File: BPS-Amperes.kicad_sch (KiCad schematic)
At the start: 36 parts, among them J1 Conn_02x10_Odd_Even, J2 ShuntConn, U1 INA186A3IDDFT, U2 OPA2196, U3 LTC2315, U4 REF1930AIDDCT

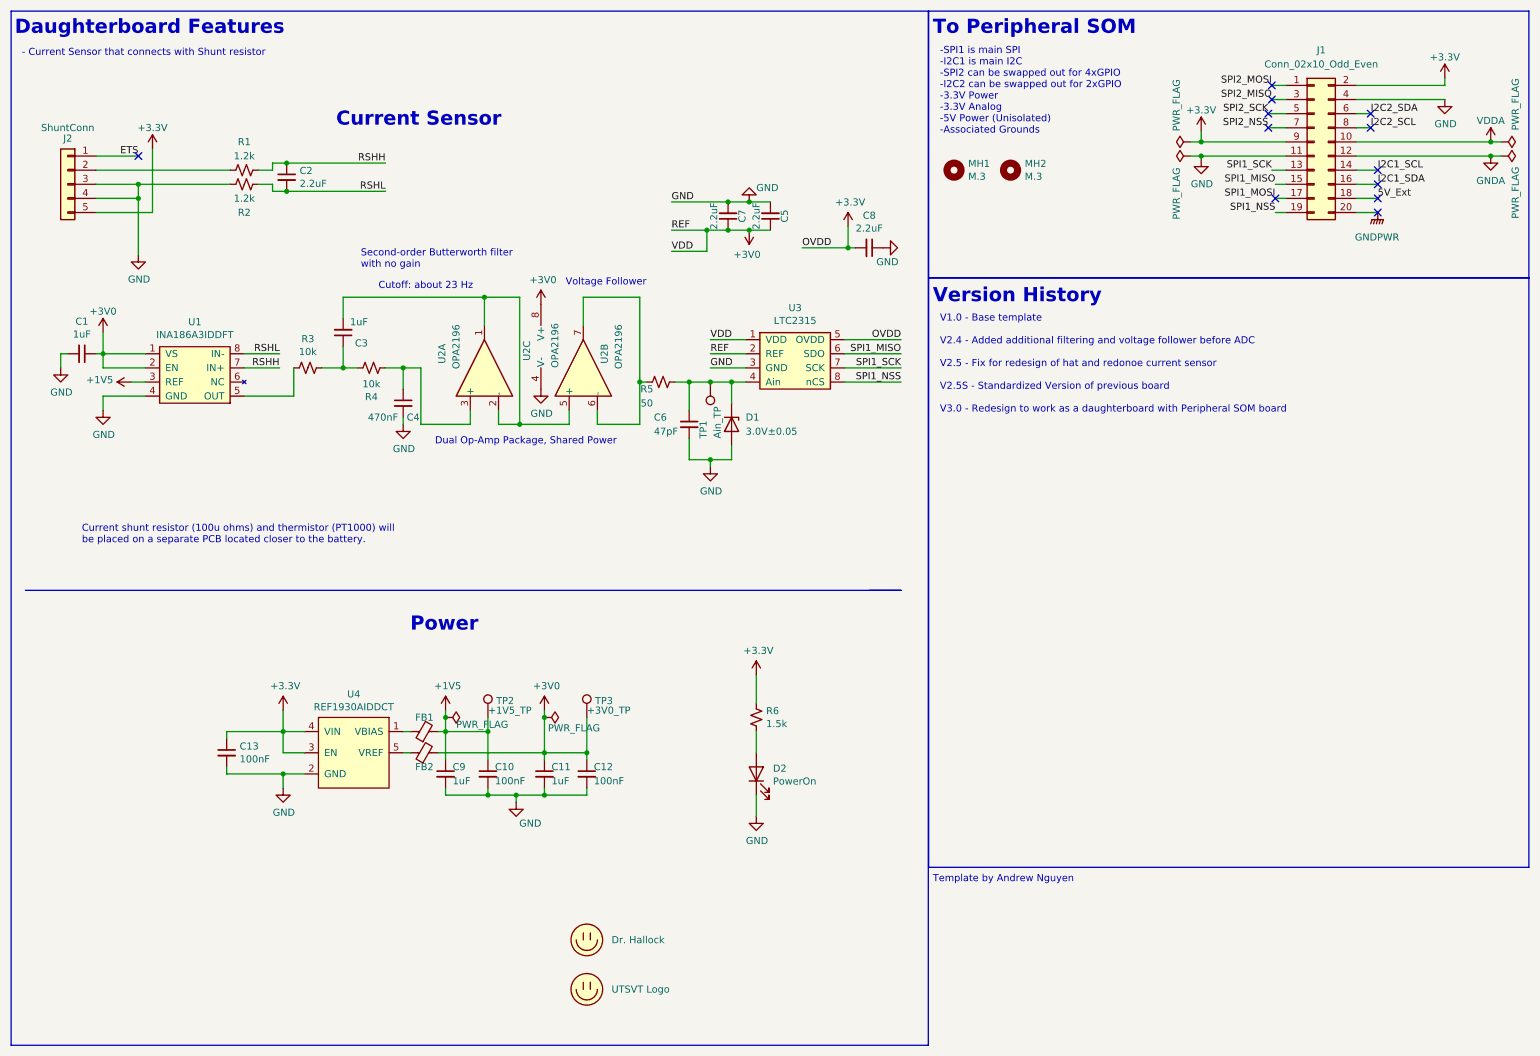
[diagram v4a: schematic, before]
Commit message: Edited a MFG part number
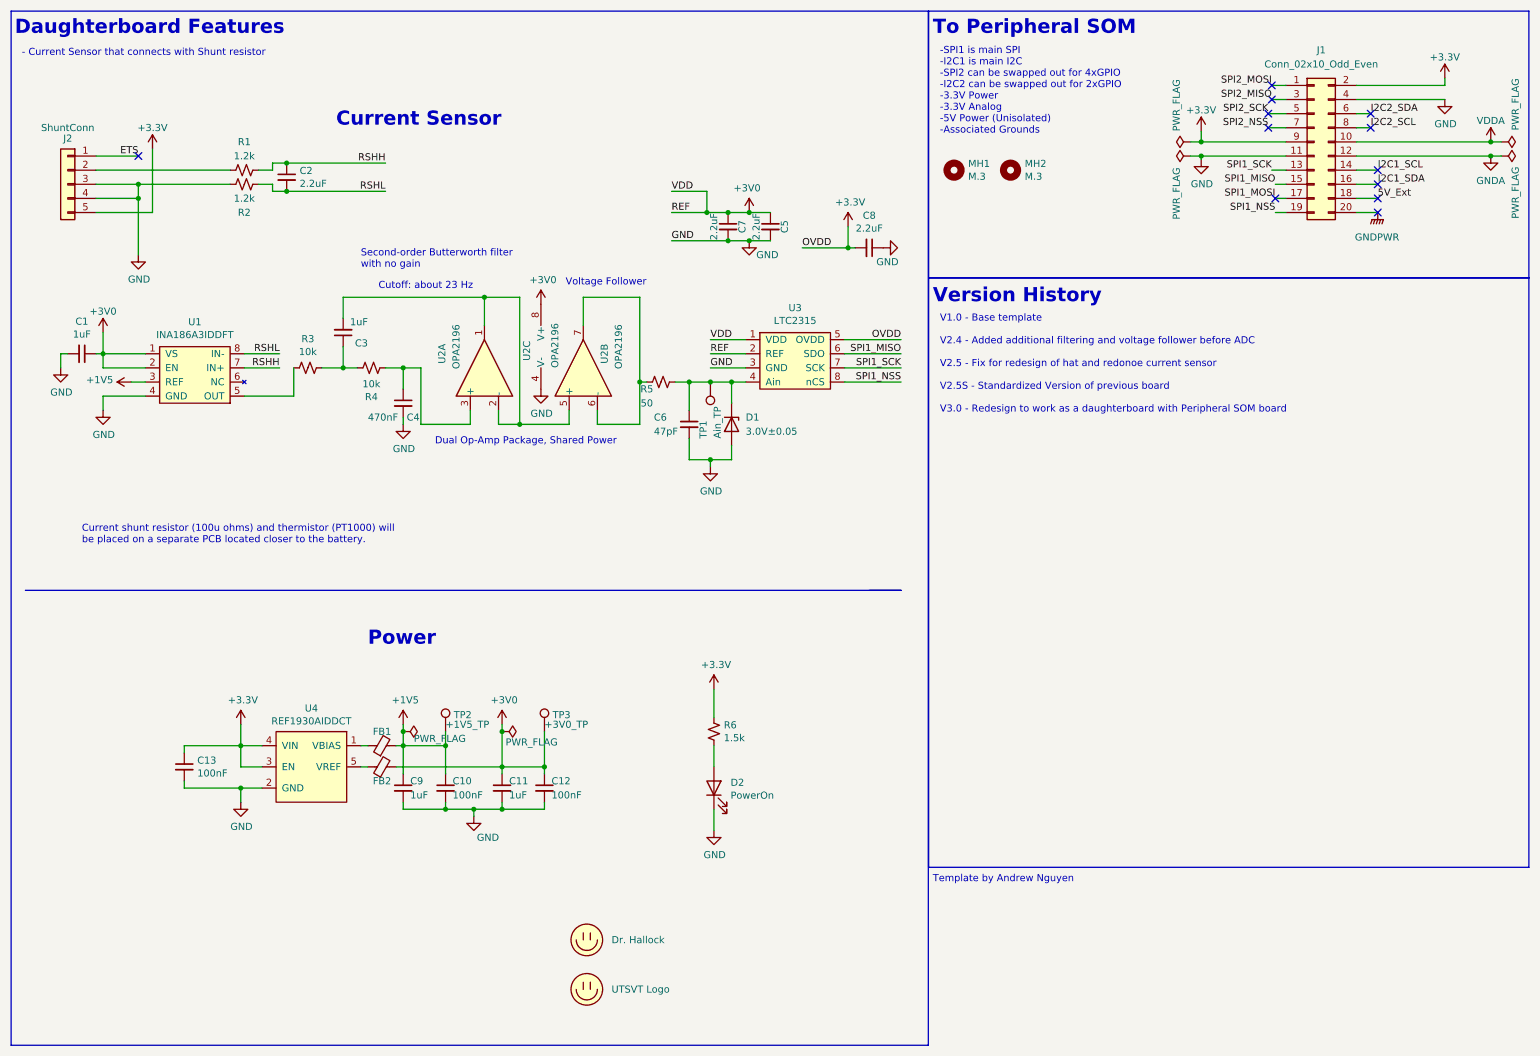
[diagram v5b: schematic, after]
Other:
- moved on the sheet: C10, C11, C12, C13, C5, C7, C9, D2, FB1, FB2, R6, TP2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

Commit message: Rearranged power lines in schematic according to recommendations for cleaner look
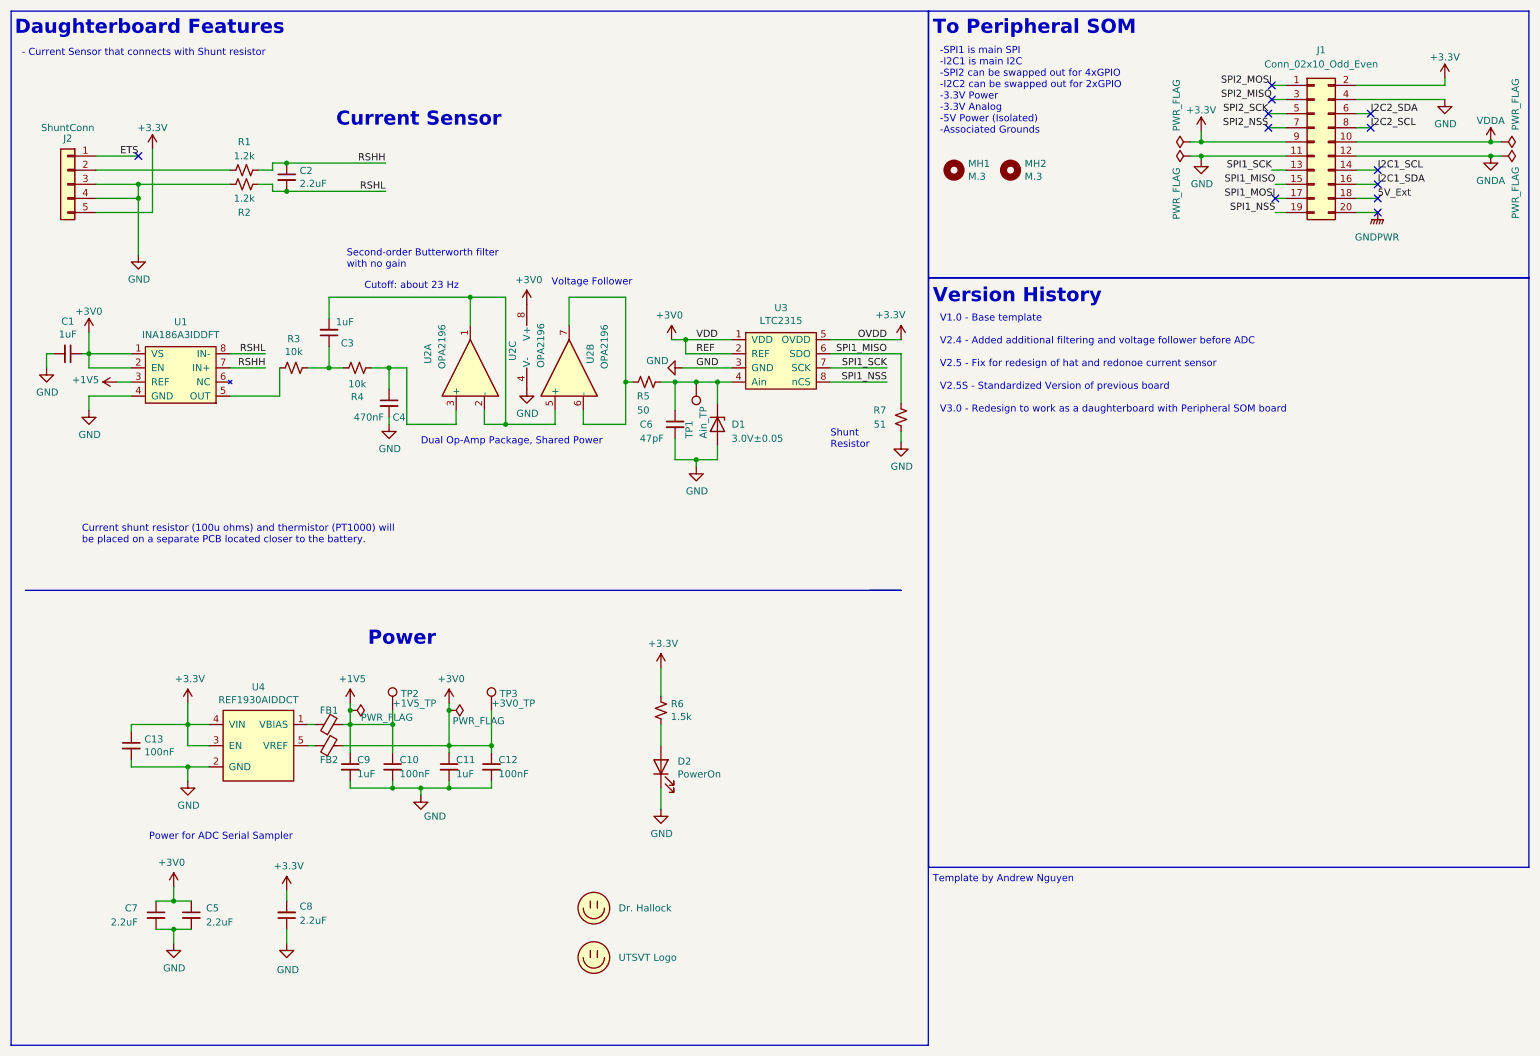
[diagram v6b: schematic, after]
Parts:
- added R7: 51, Resistor_SMD:R_0805_2012Metric, symbol Device:R_Small_US
- J1: Mfg (none) -> 53307-2071; P/N 53307-2071 -> (none)
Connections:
- net GND: now also R7.2
- net SPI1_MISO: now also R7.1
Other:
- note added: "-SPI1 is main SPI -I2C1 is main I2C -SPI2 can be swapped out for 4xGPIO -I2C2 can be swapped out for 2xGPIO -3.3V Power -3.3V Analog -5V Power (Isolated) -Associated Grounds"
- note added: "Power for ADC Serial Sampler"
- note added: "Shunt Resistor"
- note removed: "-SPI1 is main SPI -I2C1 is main I2C -SPI2 can be swapped out for 4xGPIO -I2C2 can be swapped out for 2xGPIO -3.3V Power -3.3V Analog -5V Power (Unisolated) -Associated Grounds"
- moved on the sheet: C1, C10, C11, C12, C13, C3, C4, C5, C6, C7, C8, C9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

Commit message: Updated terminating resistor orientation and location of bypass caps for ADC sampler
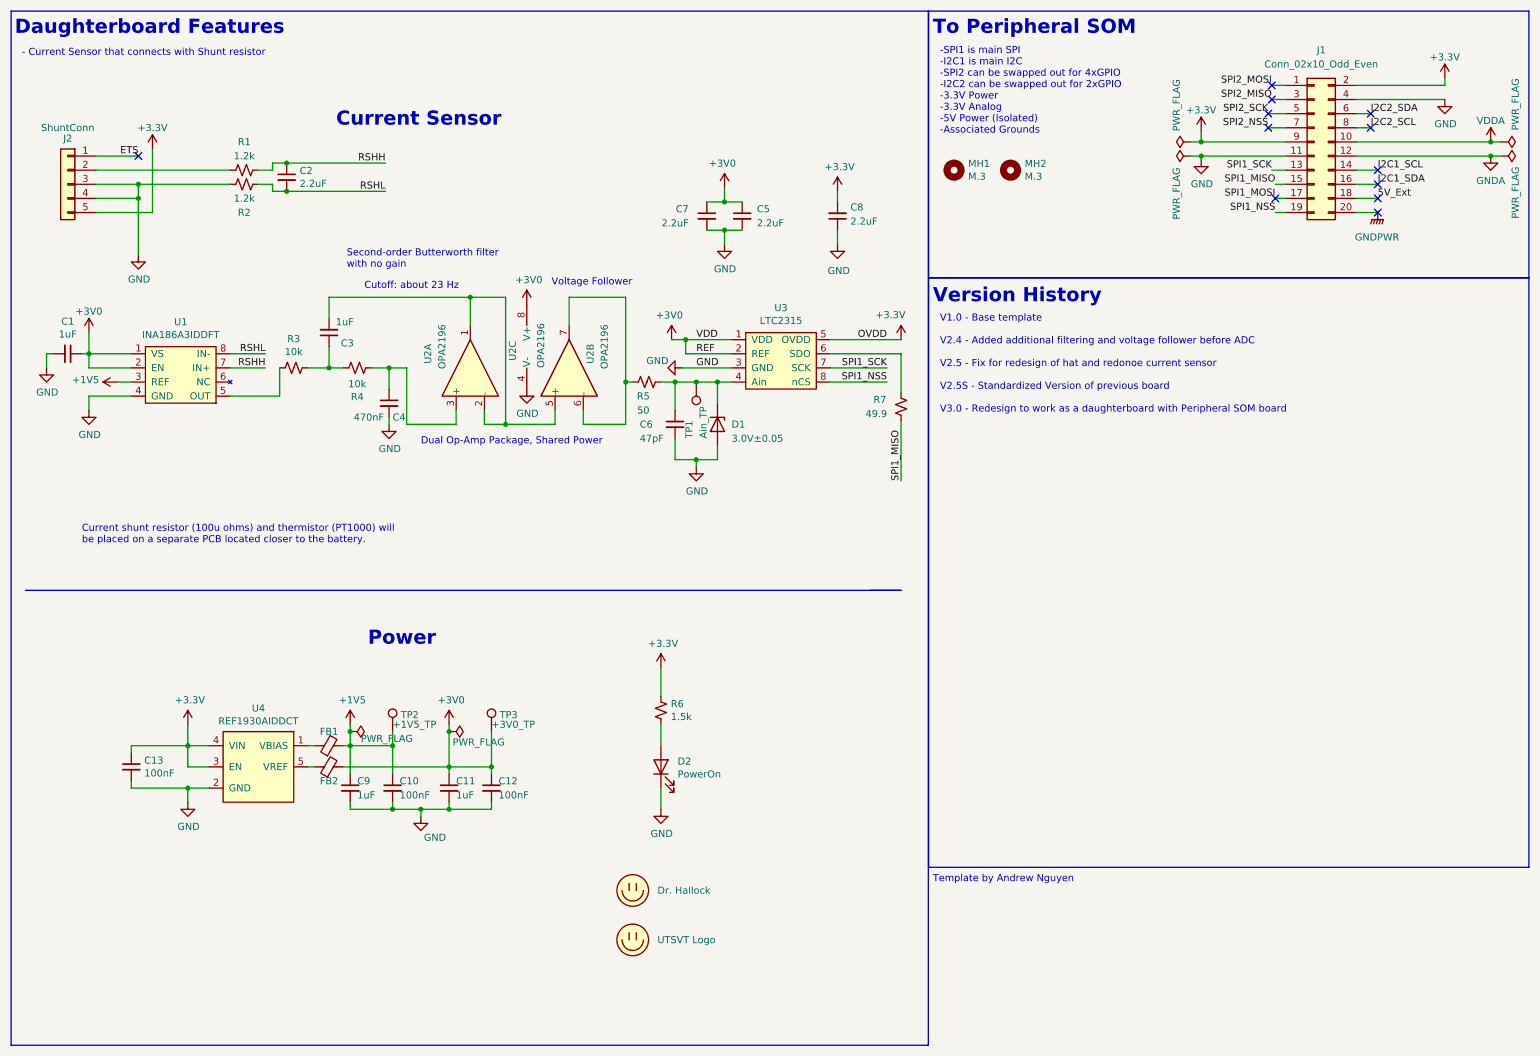
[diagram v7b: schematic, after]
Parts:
- R7: value 51 -> 49.9; Mfg ERJ-HP6D51R0V -> RCC080549R9FKEA
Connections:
- net GND: no longer R7.2
- net SPI1_MISO: no longer U3.6 (SDO)
- new net: R7.2, U3.6 (SDO)
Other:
- note removed: "Power for ADC Serial Sampler"
- note removed: "Shunt Resistor"
- moved on the sheet: C10, C11, C12, C13, C5, C7, C8, C9, FB1, FB2, R7, TP2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
